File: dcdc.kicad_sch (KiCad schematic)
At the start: 55 parts, among them J10 Conn_01x01, J11 Conn_01x01, J12 Conn_01x01, J8 Conn_01x01, J9 Conn_01x01, Q2 MMBT3904, T1 Transformer_SP_1S, U1 L78L33_SOT89, U2 TMP117, U3 LT3439, U6 LT3045xMSE, U7 24AA02-OT

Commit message: the small reset
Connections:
- net 0Vout renamed GNDf
- net 12Vout renamed 12Vf
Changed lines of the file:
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@@
     (effects (font (size 1.27 1.27)) (justify left bottom))
   )
-  (hierarchical_label "0Vout" (shape output) (at 261.62 102.87 0)
+  (hierarchical_label "GNDf" (shape output) (at 261.62 102.87 0)
     (effects (font (size 1.27 1.27)) (justify left))
   )
-  (hierarchical_label "12Vout" (shape output) (at 261.62 73.66 0)
+  (hierarchical_label "12Vf" (shape output) (at 261.62 73.66 0)
     (effects (font (size 1.27 1.27)) (justify left))
   )
-  (hierarchical_label "status" (shape input) (at 179.07 90.17 180)
+  (hierarchical_label "status" (shape output) (at 179.07 90.17 180)
     (effects (font (size 1.27 1.27)) (justify right))
   )
@@
     (effects (font (size 1.27 1.27)) (justify right))
   )
-  (hierarchical_label "Vin-" (shape input) (at 25.4 40.64 180)
+  (hierarchical_label "Ext_GND" (shape input) (at 25.4 40.64 180)
     (effects (font (size 1.27 1.27)) (justify right))
   )
@@
     (effects (font (size 1.27 1.27)) (justify right))
   )
-  (hierarchical_label "Vin+" (shape input) (at 25.4 25.4 180)
+  (hierarchical_label "Ext_Vin+" (shape input) (at 25.4 25.4 180)
     (effects (font (size 1.27 1.27)) (justify right))
   )

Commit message: net classes
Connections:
- net U3_Pin7: now reaches R5.1, U3.7 (Rt)
- net rectified+: now reaches C12.1, C14.1, D2.1 (K), D6.1 (K), Q2.3 (C), R20.2, U6.1 (IN), U6.2 (IN), U6.3 (IN), U6.4 (EN/UV)
- net U2_Pin3: now reaches R3.2, U2.3 (ALERT)
- net U2_Pin4: now reaches JP1.2 (B), JP2.2 (B), JP3.2 (B), JP4.2 (B), U2.4 (ADD0)
- net U3_Pin3: now reaches J9.1 (Pin_1), U3.3 (COLA)
- net xformer_A: now reaches D2.2 (A), D5.1 (K), J11.1 (Pin_1)
- net xformer_B: now reaches D6.2 (A), D7.1 (K), J12.1 (Pin_1)
- net status_LED: now reaches D8.2 (A), R19.2
- net U6_Pin8: now reaches C15.1, R12.1, U6.8 (SET)
- net U3_Pin4: now reaches R6.1, U3.4 (Rsl)
- net U6_Pin7: now reaches R21.2, R22.1, U6.7 (PGFB)
- net U3_Pin14: now reaches J10.1 (Pin_1), U3.14 (COLB)
- net U3_Pin6: now reaches C6.1, U3.6 (Ct)
- net U6_Pin6: now reaches R11.1, U6.6 (ILIM)
- net pwr_LED: now reaches D1.2 (A), R10.2
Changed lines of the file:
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@@
     (stroke (width 0) (type default) (color 0 0 0 0))
+  )
+  (label "U3_Pin7" (at 54.61 99.06 180)
+    (effects (font (size 0.5 0.5)) (justify right bottom))
+  )
+  (label "pwr_LED" (at 50.8 25.4 180)
+    (effects (font (size 0.5 0.5)) (justify right bottom))
+  )
+  (label "xformer_A" (at 130.81 73.66 180)
+    (effects (font (size 0.5 0.5)) (justify right bottom))
+  )
+  (label "U2_Pin3" (at 144.78 153.67 180)
+    (effects (font (size 0.5 0.5)) (justify right bottom))
+  )
+  (label "U6_Pin6" (at 200.66 78.74 0)
+    (effects (font (size 0.5 0.5)) (justify left bottom))
+  )
+  (label "U6_Pin8" (at 208.28 81.28 0)
+    (effects (font (size 0.5 0.5)) (justify left bottom))
+  )
+  (label "U3_Pin3" (at 80.01 83.82 0)
+    (effects (font (size 0.5 0.5)) (justify left bottom))
+  )
+  (label "U6_Pin7" (at 245.11 78.74 180)
+    (effects (font (size 0.5 0.5)) (justify right bottom))
+  )
+  (label "U3_Pin4" (at 80.2368 99.06 0)
+    (effects (font (size 0.5 0.5)) (justify left bottom))
   )
   (label "PG" (at 242.57 91.44 180)
     (effects (font (size 1.27 1.27)) (justify right bottom))
   )
+  (label "U3_Pin14" (at 80.01 91.44 0)
+    (effects (font (size 0.5 0.5)) (justify left bottom))
+  )
+  (label "rectified+" (at 143.51 73.66 0)
+    (effects (font (size 0.5 0.5)) (justify left bottom))
+  )
+  (label "status_LED" (at 186.69 90.17 0)
+    (effects (font (size 0.5 0.5)) (justify left bottom))
+  )
+  (label "xformer_B" (at 130.81 102.87 180)
+    (effects (font (size 0.5 0.5)) (justify right bottom))
+  )
   (label "PG" (at 194.31 83.82 0)
     (effects (font (size 1.27 1.27)) (justify left bottom))
   )
+  (label "U3_Pin6" (at 48.26 96.52 180)
+    (effects (font (size 0.5 0.5)) (justify right bottom))
+  )
+  (label "U2_Pin4" (at 118.11 161.29 180)
+    (effects (font (size 0.5 0.5)) (justify right bottom))
+  )
   (hierarchical_label "GNDf" (shape output) (at 261.62 102.87 0)

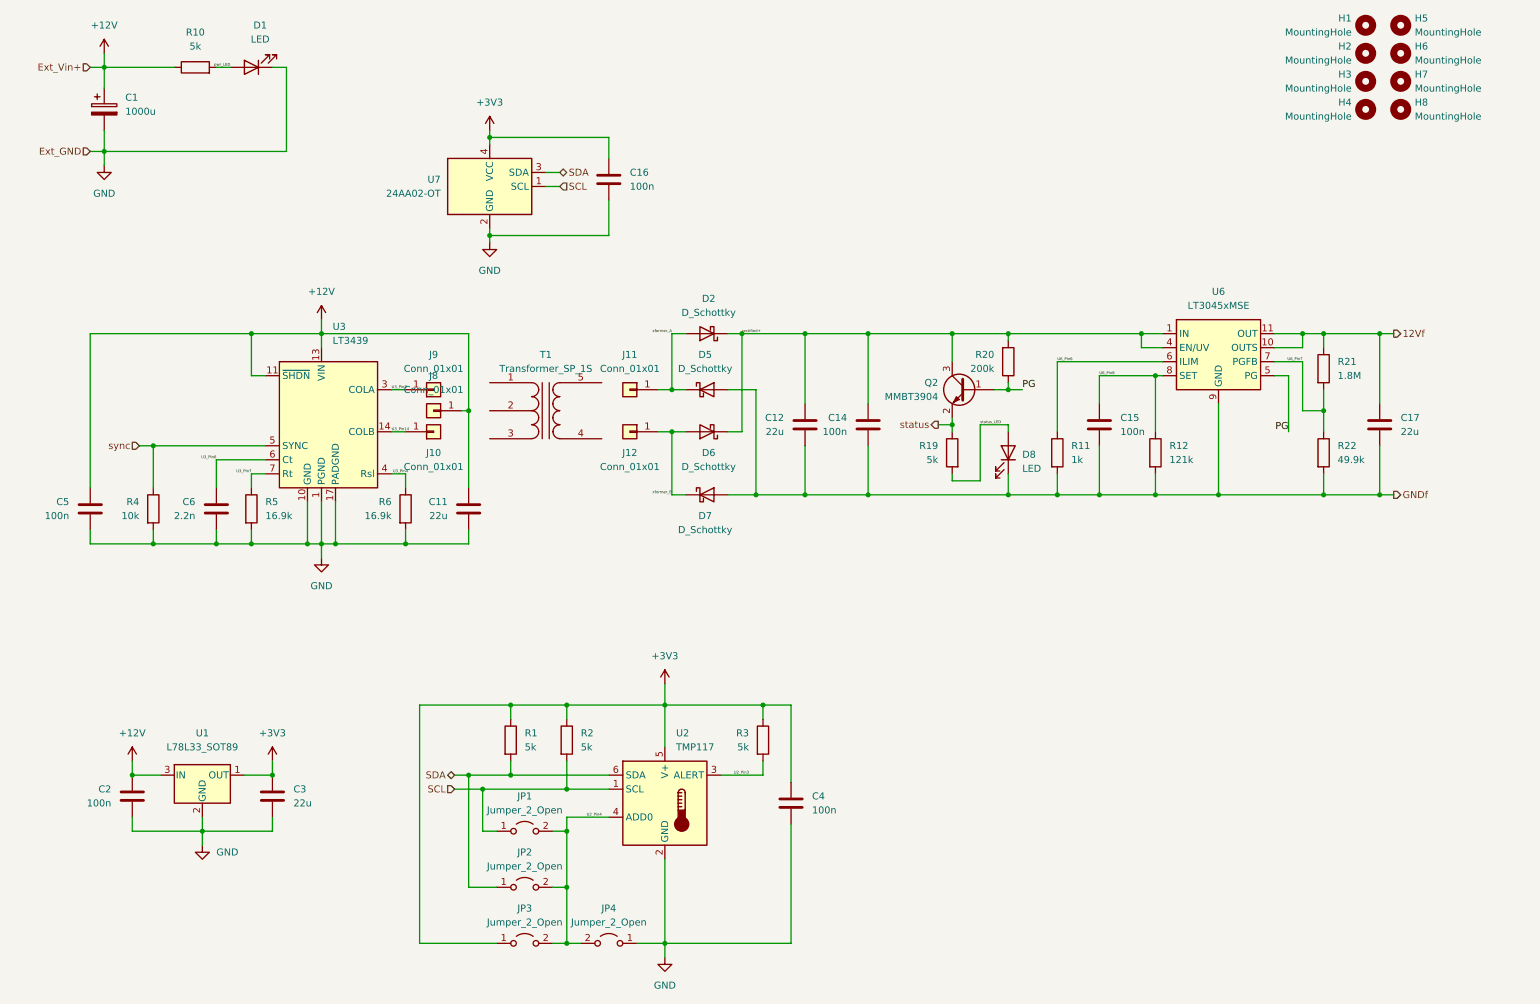
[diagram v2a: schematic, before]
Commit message: reference designators reassigned
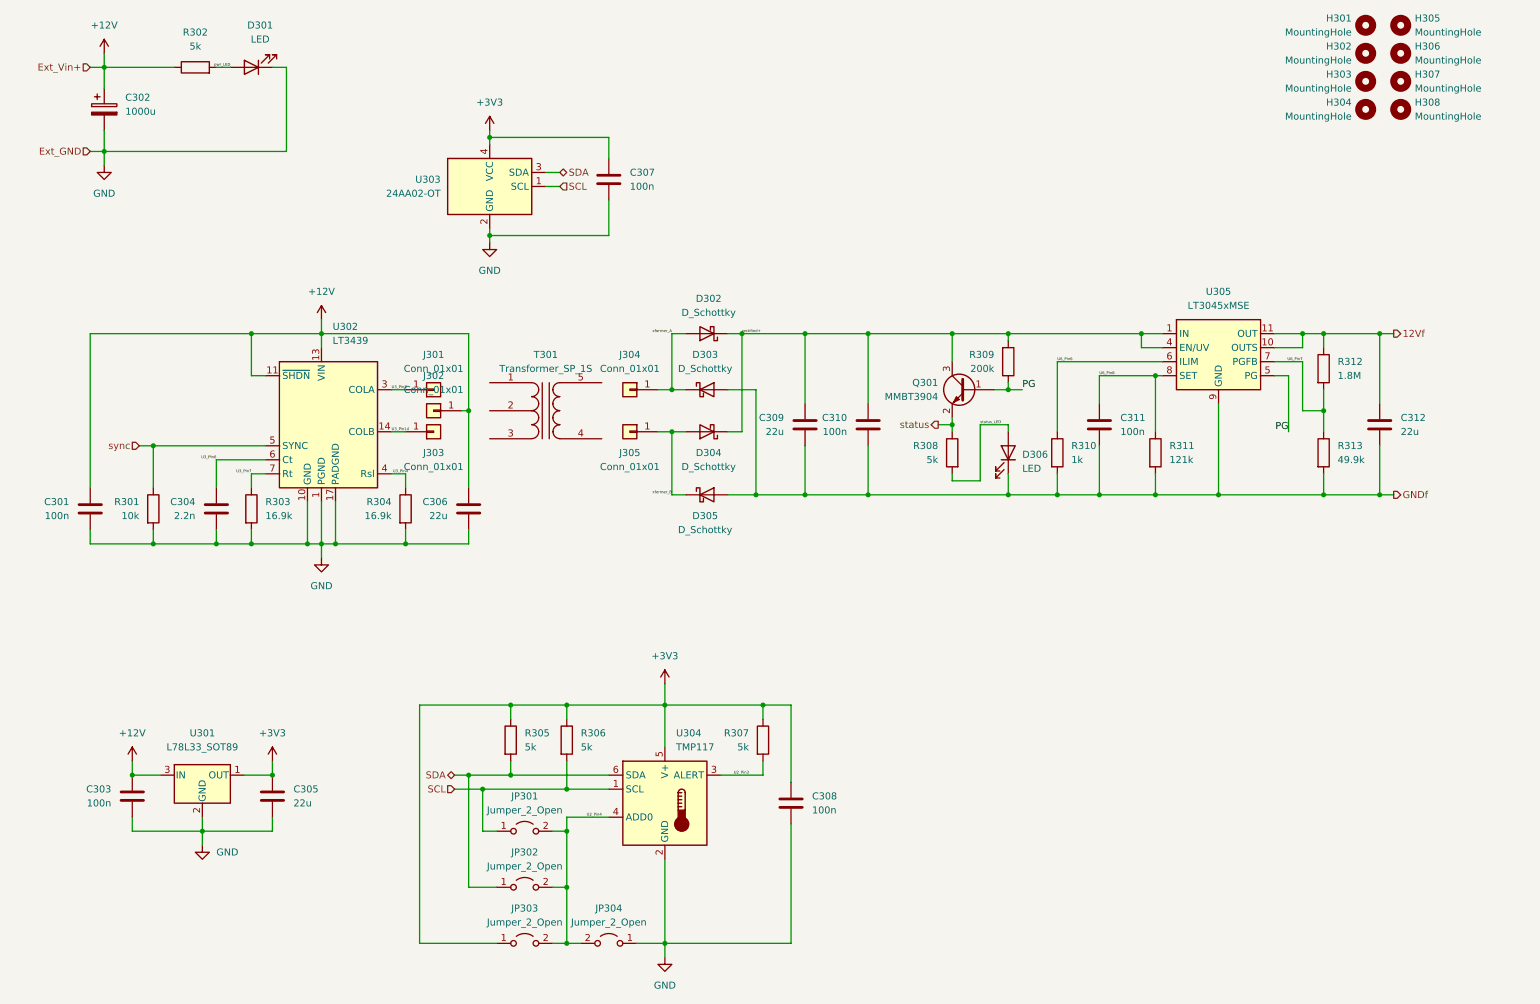
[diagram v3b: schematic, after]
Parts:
- renumbered C5 to C301, C1 to C302, C2 to C303, C6 to C304, C3 to C305, C11 to C306, C16 to C307, C4 to C308, C12 to C309, C14 to C310, C15 to C311, C17 to C312, D1 to D301, D2 to D302, D5 to D303, D6 to D304, D7 to D305, D8 to D306, H1 to H301, H2 to H302, H3 to H303, H4 to H304, H5 to H305, H6 to H306, H7 to H307, H8 to H308, J9 to J301, J8 to J302, J10 to J303, J11 to J304, J12 to J305, JP1 to JP301, JP2 to JP302, JP3 to JP303, JP4 to JP304, Q2 to Q301, R4 to R301, R10 to R302, R5 to R303, R6 to R304, R1 to R305, R2 to R306, R3 to R307, R19 to R308, R20 to R309, R11 to R310, R12 to R311, R21 to R312, R22 to R313, T1 to T301, U1 to U301, U3 to U302, U7 to U303, U2 to U304, U6 to U305

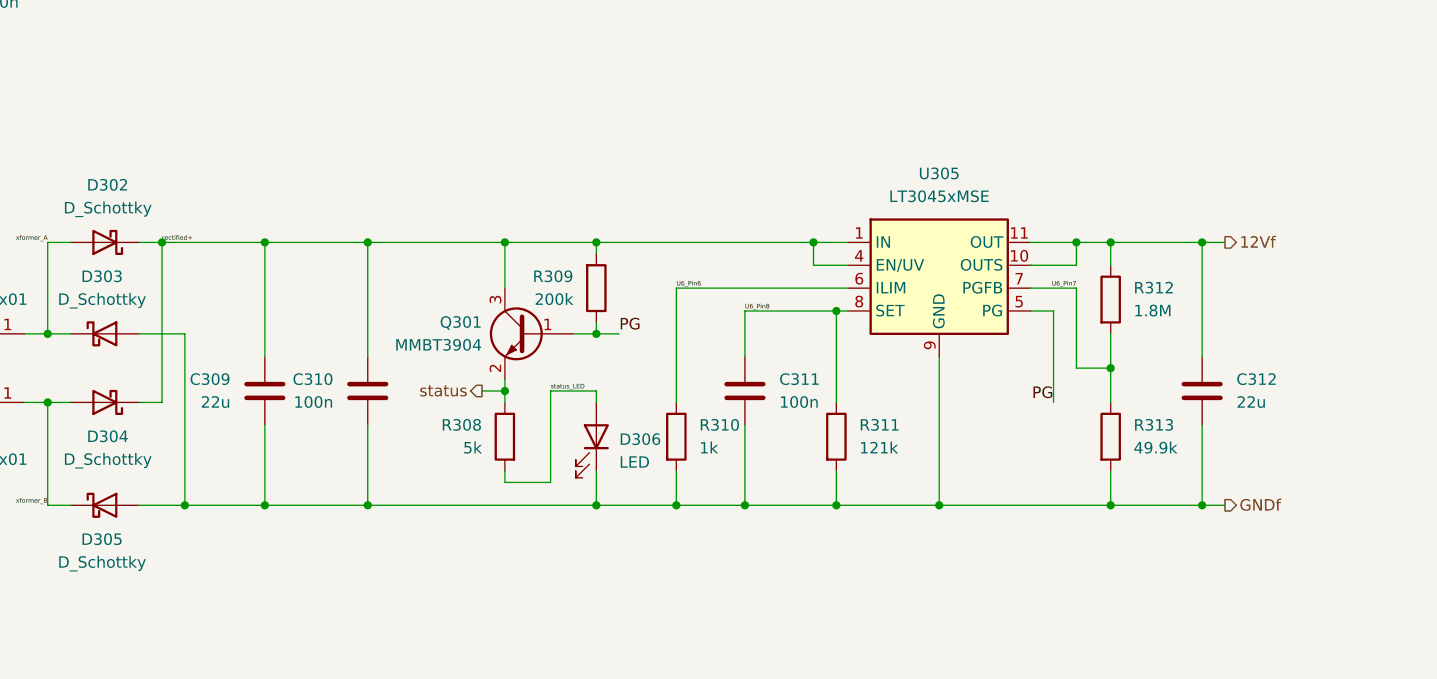
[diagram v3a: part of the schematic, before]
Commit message: added common mode filter
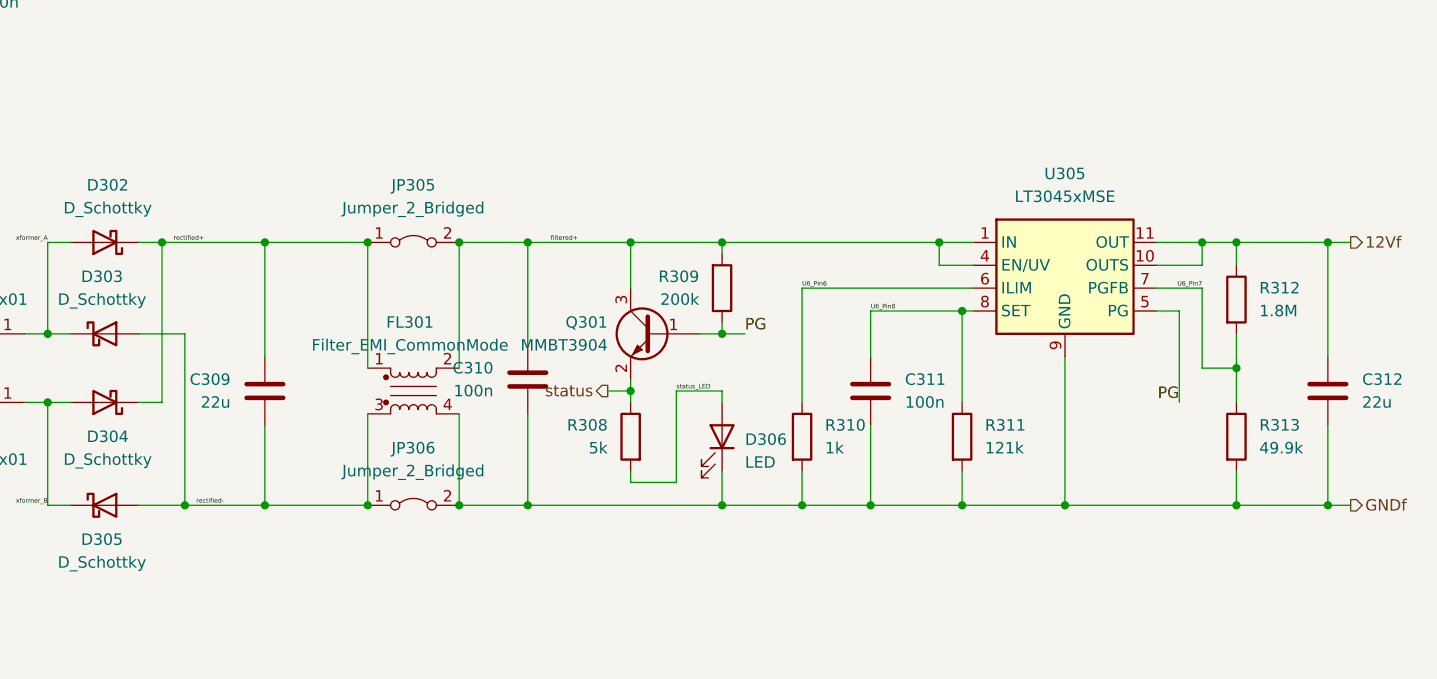
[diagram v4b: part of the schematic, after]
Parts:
- added FL301: Filter_EMI_CommonMode, ADRmu_Library:Filter_EPCOS_B82793C0, symbol Device:Filter_EMI_CommonMode
- added JP305, JP306: Jumper_2_Bridged, Jumper:SolderJumper-2_P1.3mm_Bridged_RoundedPad1.0x1.5mm, symbol Jumper:Jumper_2_Bridged
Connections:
- net GNDf: now also FL301.4, JP306.2 (B); no longer C309.2, D303.2 (A), D305.2 (A)
- net rectified+: now also FL301.1, JP305.1 (A); no longer C310.1, Q301.3 (C), R309.2, U305.1 (IN), U305.2 (IN), U305.3 (IN), U305.4 (EN/UV)
- new net filtered+: C310.1, FL301.2, JP305.2 (B), Q301.3 (C), R309.2, U305.1 (IN), U305.2 (IN), U305.3 (IN), U305.4 (EN/UV)
- new net rectified-: C309.2, D303.2 (A), D305.2 (A), FL301.3, JP306.1 (A)
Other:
- moved on the sheet: C310, C311, C312, D306, Q301, R308, R309, R310, R311, R312, R313, U305

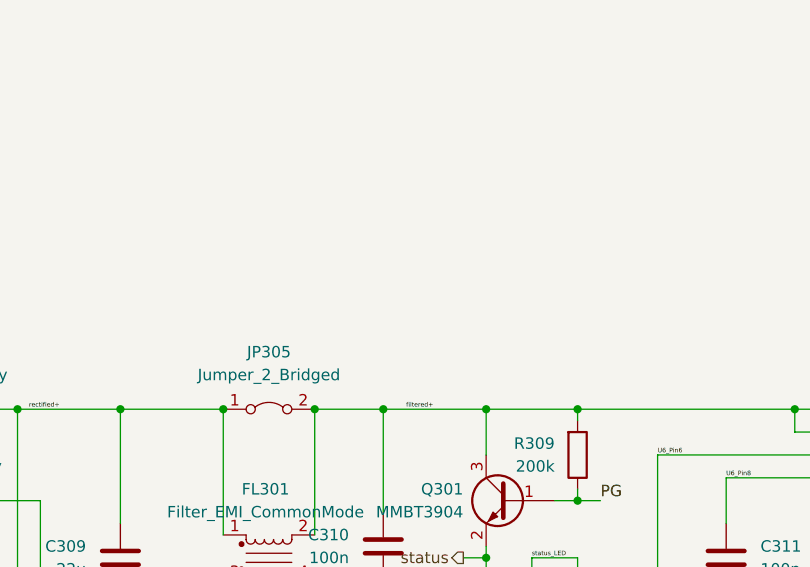
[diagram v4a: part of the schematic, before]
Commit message: Obligatory bugs in the first production run:
- Missing stability cap between buffer out and -in
- Missing cap for autozeroing buffer
- Side status LEDs need to be flipped
- Many schematic net names wrong
- LDO power good implemented wrong
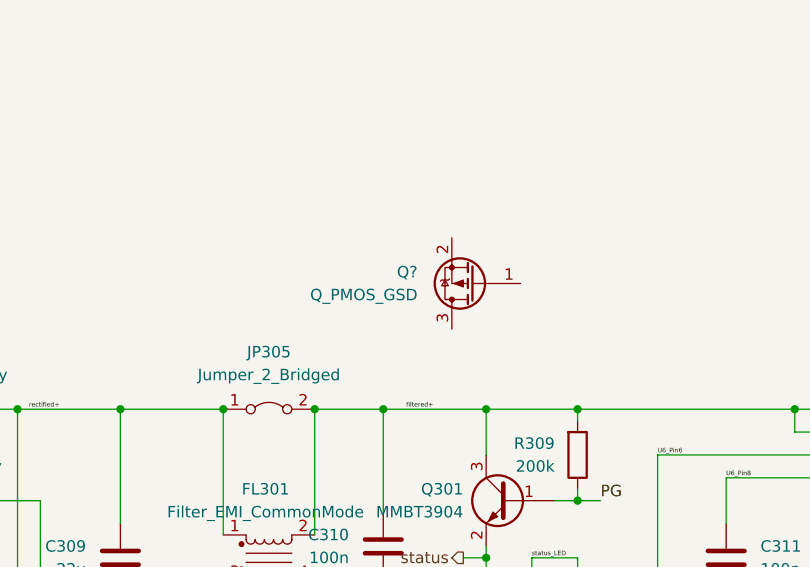
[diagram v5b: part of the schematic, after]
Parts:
- added Q?: Q_PMOS_GSD, symbol Device:Q_PMOS_GSD
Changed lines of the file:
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@@
     (pin "2")
   )
+  (symbol (lib_id "Device:Q_PMOS_GSD") (at 194.31 59.69 180) (unit 1)
+    (in_bom yes) (on_board yes) (fields_autoplaced)
+    (property "Reference" "Q?" (id 0) (at 187.96 58.4199 0)
+      (effects (font (size 1.27 1.27)) (justify left))
+    )
+    (property "Value" "Q_PMOS_GSD" (id 1) (at 187.96 60.9599 0)
+      (effects (font (size 1.27 1.27)) (justify left))
+    )
+    (property "Footprint" "" (id 2) (at 189.23 62.23 0)
+      (effects (font (size 1.27 1.27)) hide)
+    )
+    (property "Datasheet" "~" (id 3) (at 194.31 59.69 0)
+      (effects (font (size 1.27 1.27)) hide)
+    )
+    (pin "1")
+    (pin "2")
+    (pin "3")
+  )
 )

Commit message: GNDf terminal was sharing a via with heater return
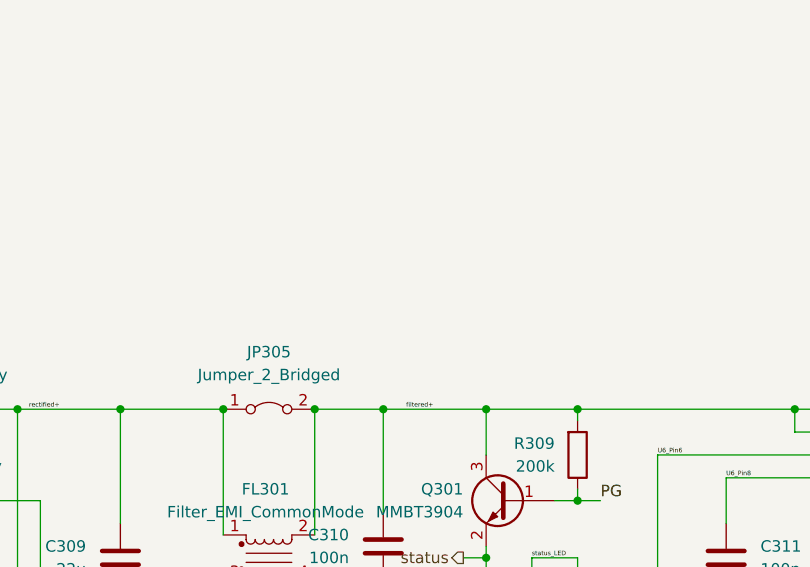
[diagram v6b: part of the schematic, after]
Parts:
- removed Q?: Q_PMOS_GSD, symbol Device:Q_PMOS_GSD
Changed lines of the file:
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@@
     (pin "2")
   )
-  (symbol (lib_id "Device:Q_PMOS_GSD") (at 194.31 59.69 180) (unit 1)
-    (in_bom yes) (on_board yes) (fields_autoplaced)
-    (property "Reference" "Q?" (id 0) (at 187.96 58.4199 0)
-      (effects (font (size 1.27 1.27)) (justify left))
-    )
-    (property "Value" "Q_PMOS_GSD" (id 1) (at 187.96 60.9599 0)
-      (effects (font (size 1.27 1.27)) (justify left))
-    )
-    (property "Footprint" "" (id 2) (at 189.23 62.23 0)
-      (effects (font (size 1.27 1.27)) hide)
-    )
-    (property "Datasheet" "~" (id 3) (at 194.31 59.69 0)
-      (effects (font (size 1.27 1.27)) hide)
-    )
-    (pin "1")
-    (pin "2")
-    (pin "3")
-  )
 )
